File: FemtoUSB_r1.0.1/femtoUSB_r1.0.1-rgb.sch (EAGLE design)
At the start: 33 parts, among them IC1 ATSAMD21E18A-MUT

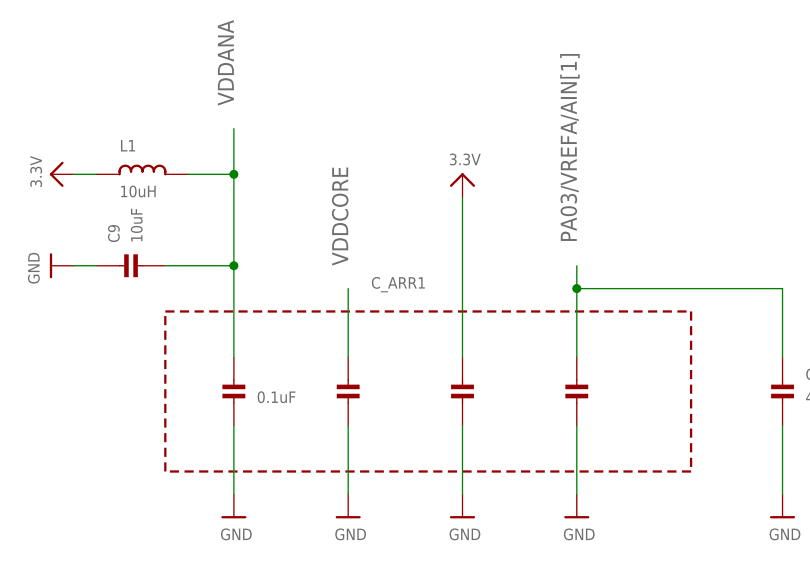
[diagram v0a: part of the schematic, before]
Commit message: Updating FemtoUSB r1.0.1 w/ RGB. Silkscreen updated to reflect Arduino pin assignments
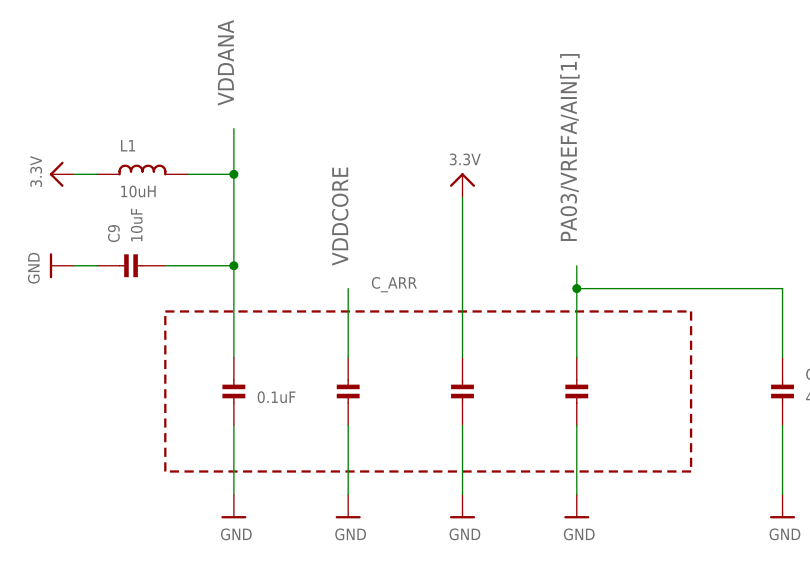
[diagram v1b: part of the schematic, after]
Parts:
- renumbered C_ARR1 to C_ARR, U$40 to OSC32K, U$43 to BTN_BOOT
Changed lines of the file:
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@@
 <part name="U$18" library="microbuilder" deviceset="GND" device=""/>
 <part name="U$19" library="microbuilder" deviceset="3.3V" device=""/>
-<part name="C_ARR1" library="array-capacitor" deviceset="KEMET_CERAMIC_CAPACITOR_ARRAY_1X4" device="" value="0.1uF"/>
+<part name="C_ARR" library="array-capacitor" deviceset="KEMET_CERAMIC_CAPACITOR_ARRAY_1X4" device="" value="0.1uF"/>
 <part name="SJ_RESET" library="femtoduino" deviceset="SPST_SMD" device="" value="OMRON B3U-300P(M)"/>
 <part name="U$17" library="microbuilder" deviceset="GND" device=""/>
@@
 <part name="C8" library="microbuilder" deviceset="CAP_CERAMIC" device="_0402MP" value="10uF"/>
 <part name="U$39" library="microbuilder" deviceset="GND" device=""/>
-<part name="U$40" library="crystals" deviceset="ABS06-107-32.768KHZ-T" device=""/>
+<part name="OSC32K" library="crystals" deviceset="ABS06-107-32.768KHZ-T" device=""/>
 <part name="C10" library="microbuilder" deviceset="CAP_CERAMIC" device="_0402MP" value="12pF"/>
 <part name="C11" library="microbuilder" deviceset="CAP_CERAMIC" device="_0402MP" value="12pF"/>
 <part name="U$41" library="microbuilder" deviceset="GND" device=""/>
 <part name="U$42" library="microbuilder" deviceset="GND" device=""/>
-<part name="U$43" library="omron_tactile_switch" deviceset="TACTILE_SWITCH_NO_GND_NO_BOSS" device=""/>
+<part name="BTN_BOOT" library="omron_tactile_switch" deviceset="TACTILE_SWITCH_NO_GND_NO_BOSS" device=""/>
 <part name="R5" library="microbuilder" deviceset="RESISTOR" device="_0402MP" value="330"/>
 <part name="R6" library="microbuilder" deviceset="RESISTOR" device="_0402MP" value="100K"/>
@@
 <instance part="U$18" gate="G$1" x="226.06" y="134.62"/>
 <instance part="U$19" gate="G$1" x="226.06" y="177.8"/>
-<instance part="C_ARR1" gate="G$1" x="180.34" y="58.42"/>
+<instance part="C_ARR" gate="G$1" x="180.34" y="58.42"/>
 <instance part="SJ_RESET" gate="G$1" x="200.66" y="147.32" rot="MR270"/>
 <instance part="U$17" gate="G$1" x="22.86" y="142.24" rot="R270"/>
@@
 <instance part="C8" gate="G$1" x="241.3" y="58.42" rot="R180"/>
 <instance part="U$39" gate="G$1" x="172.72" y="152.4" rot="R90"/>
-<instance part="U$40" gate="G$1" x="152.4" y="137.16"/>
+<instance part="OSC32K" gate="G$1" x="152.4" y="137.16"/>
 <instance part="C10" gate="G$1" x="147.32" y="132.08" rot="R180"/>
 <instance part="C11" gate="G$1" x="162.56" y="132.08" rot="R180"/>
 <instance part="U$41" gate="G$1" x="147.32" y="121.92"/>
 <instance part="U$42" gate="G$1" x="162.56" y="121.92"/>
-<instance part="U$43" gate="G$1" x="154.94" y="152.4"/>
+<instance part="BTN_BOOT" gate="G$1" x="154.94" y="152.4"/>
 <instance part="R5" gate="G$1" x="33.02" y="83.82"/>
 <instance part="R6" gate="G$1" x="43.18" y="78.74"/>
@@
 </segment>
 <segment>
-<pinref part="U$40" gate="G$1" pin="XTALIN"/>
+<pinref part="OSC32K" gate="G$1" pin="XTALIN"/>
 <wire x1="152.4" y1="137.16" x2="147.32" y2="137.16" width="0.1524" layer="91"/>
 <label x="134.62" y="139.7" size="1.778" layer="95"/>
@@
 </segment>
 <segment>
-<pinref part="U$40" gate="G$1" pin="XTALOUT"/>
+<pinref part="OSC32K" gate="G$1" pin="XTALOUT"/>
 <wire x1="157.48" y1="137.16" x2="162.56" y2="137.16" width="0.1524" layer="91"/>
 <label x="167.64" y="139.7" size="1.778" layer="95"/>
@@
 </segment>
 <segment>
-<pinref part="C_ARR1" gate="G$1" pin="P$7"/>
+<pinref part="C_ARR" gate="G$1" pin="P$7"/>
 <wire x1="198.12" y1="60.96" x2="198.12" y2="68.58" width="0.1524" layer="91"/>
 <label x="198.12" y="73.66" size="1.778" layer="95" rot="R90"/>
@@
 </segment>
 <segment>
-<pinref part="C_ARR1" gate="G$1" pin="P$1"/>
+<pinref part="C_ARR" gate="G$1" pin="P$1"/>
 <wire x1="160.02" y1="60.96" x2="160.02" y2="71.12" width="0.1524" layer="91"/>
 <label x="160.02" y="88.9" size="1.778" layer="95" rot="R90"/>
@@
 <segment>
 <label x="144.78" y="152.4" size="1.778" layer="95" rot="R180"/>
-<pinref part="U$43" gate="G$1" pin="1"/>
+<pinref part="BTN_BOOT" gate="G$1" pin="1"/>
 <wire x1="147.32" y1="152.4" x2="152.4" y2="152.4" width="0.1524" layer="91"/>
 </segment>
@@
 </segment>
 <segment>
-<pinref part="C_ARR1" gate="G$1" pin="P$3"/>
+<pinref part="C_ARR" gate="G$1" pin="P$3"/>
 <wire x1="172.72" y1="60.96" x2="172.72" y2="68.58" width="0.1524" layer="91"/>
 <label x="172.72" y="71.12" size="1.778" layer="95" rot="R90"/>
@@
 </segment>
 <segment>
-<pinref part="C_ARR1" gate="G$1" pin="P$2"/>
+<pinref part="C_ARR" gate="G$1" pin="P$2"/>
 <pinref part="U$22" gate="G$1" pin="GND"/>
 <wire x1="160.02" y1="45.72" x2="160.02" y2="53.34" width="0.1524" layer="91"/>
 </segment>
 <segment>
-<pinref part="C_ARR1" gate="G$1" pin="P$4"/>
+<pinref part="C_ARR" gate="G$1" pin="P$4"/>
 <pinref part="U$23" gate="G$1" pin="GND"/>
 <wire x1="172.72" y1="45.72" x2="172.72" y2="53.34" width="0.1524" layer="91"/>
 </segment>
 <segment>
-<pinref part="C_ARR1" gate="G$1" pin="P$6"/>
+<pinref part="C_ARR" gate="G$1" pin="P$6"/>
 <pinref part="U$24" gate="G$1" pin="GND"/>
 <wire x1="185.42" y1="45.72" x2="185.42" y2="53.34" width="0.1524" layer="91"/>
@@
 </segment>
 <segment>
-<pinref part="C_ARR1" gate="G$1" pin="P$8"/>
+<pinref part="C_ARR" gate="G$1" pin="P$8"/>
 <wire x1="198.12" y1="53.34" x2="198.12" y2="45.72" width="0.1524" layer="91"/>
 <pinref part="U$33" gate="G$1" pin="GND"/>
@@
 <pinref part="U$39" gate="G$1" pin="GND"/>
 <wire x1="162.56" y1="152.4" x2="170.18" y2="152.4" width="0.1524" layer="91"/>
-<pinref part="U$43" gate="G$1" pin="2"/>
+<pinref part="BTN_BOOT" gate="G$1" pin="2"/>
 </segment>
 <segment>
@@
 </segment>
 <segment>
-<pinref part="C_ARR1" gate="G$1" pin="P$5"/>
+<pinref part="C_ARR" gate="G$1" pin="P$5"/>
 <wire x1="185.42" y1="60.96" x2="185.42" y2="78.74" width="0.1524" layer="91"/>
 <pinref part="U$2" gate="G$1" pin="3.3V"/>

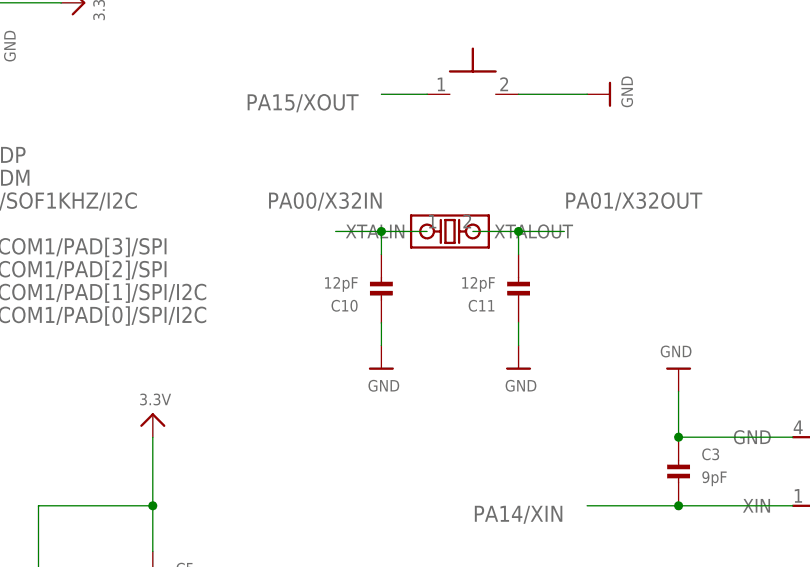
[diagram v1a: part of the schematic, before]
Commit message: Updating cap value for 32.768KHz crystal to correct value, adding in example sketches
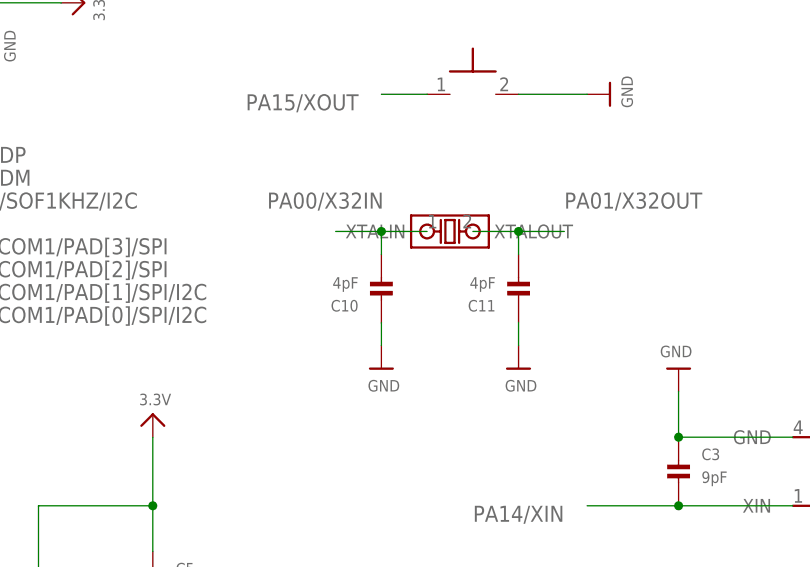
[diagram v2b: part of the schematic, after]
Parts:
- C10, C11: value 12pF -> 4pF
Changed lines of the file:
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@@
 <part name="U$39" library="microbuilder" deviceset="GND" device=""/>
 <part name="OSC32K" library="crystals" deviceset="ABS06-107-32.768KHZ-T" device=""/>
-<part name="C10" library="microbuilder" deviceset="CAP_CERAMIC" device="_0402MP" value="12pF"/>
-<part name="C11" library="microbuilder" deviceset="CAP_CERAMIC" device="_0402MP" value="12pF"/>
+<part name="C10" library="microbuilder" deviceset="CAP_CERAMIC" device="_0402MP" value="4pF"/>
+<part name="C11" library="microbuilder" deviceset="CAP_CERAMIC" device="_0402MP" value="4pF"/>
 <part name="U$41" library="microbuilder" deviceset="GND" device=""/>
 <part name="U$42" library="microbuilder" deviceset="GND" device=""/>

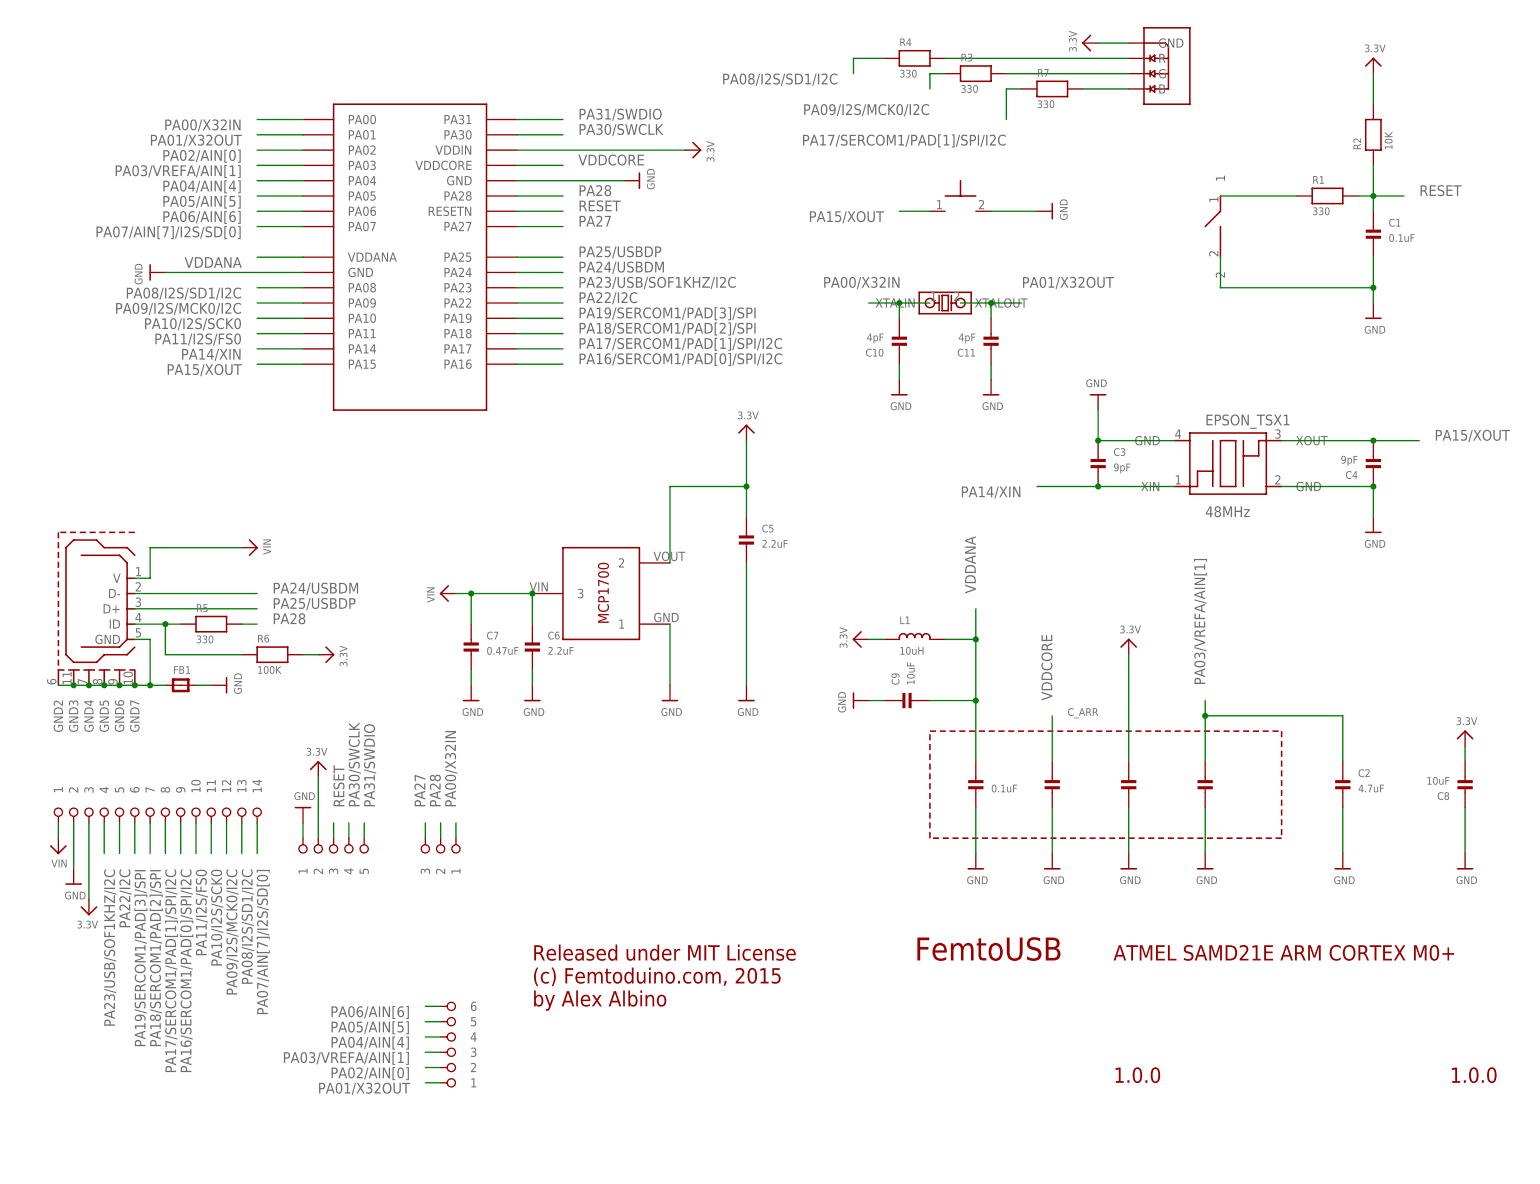
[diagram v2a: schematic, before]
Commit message: Updating Bill of Materials, and component attributes to include mfr ID. Button is now used by PA27 instead of PA15 (boot), since Arduino core doesn't need the boot pin to upload subsequent sketches
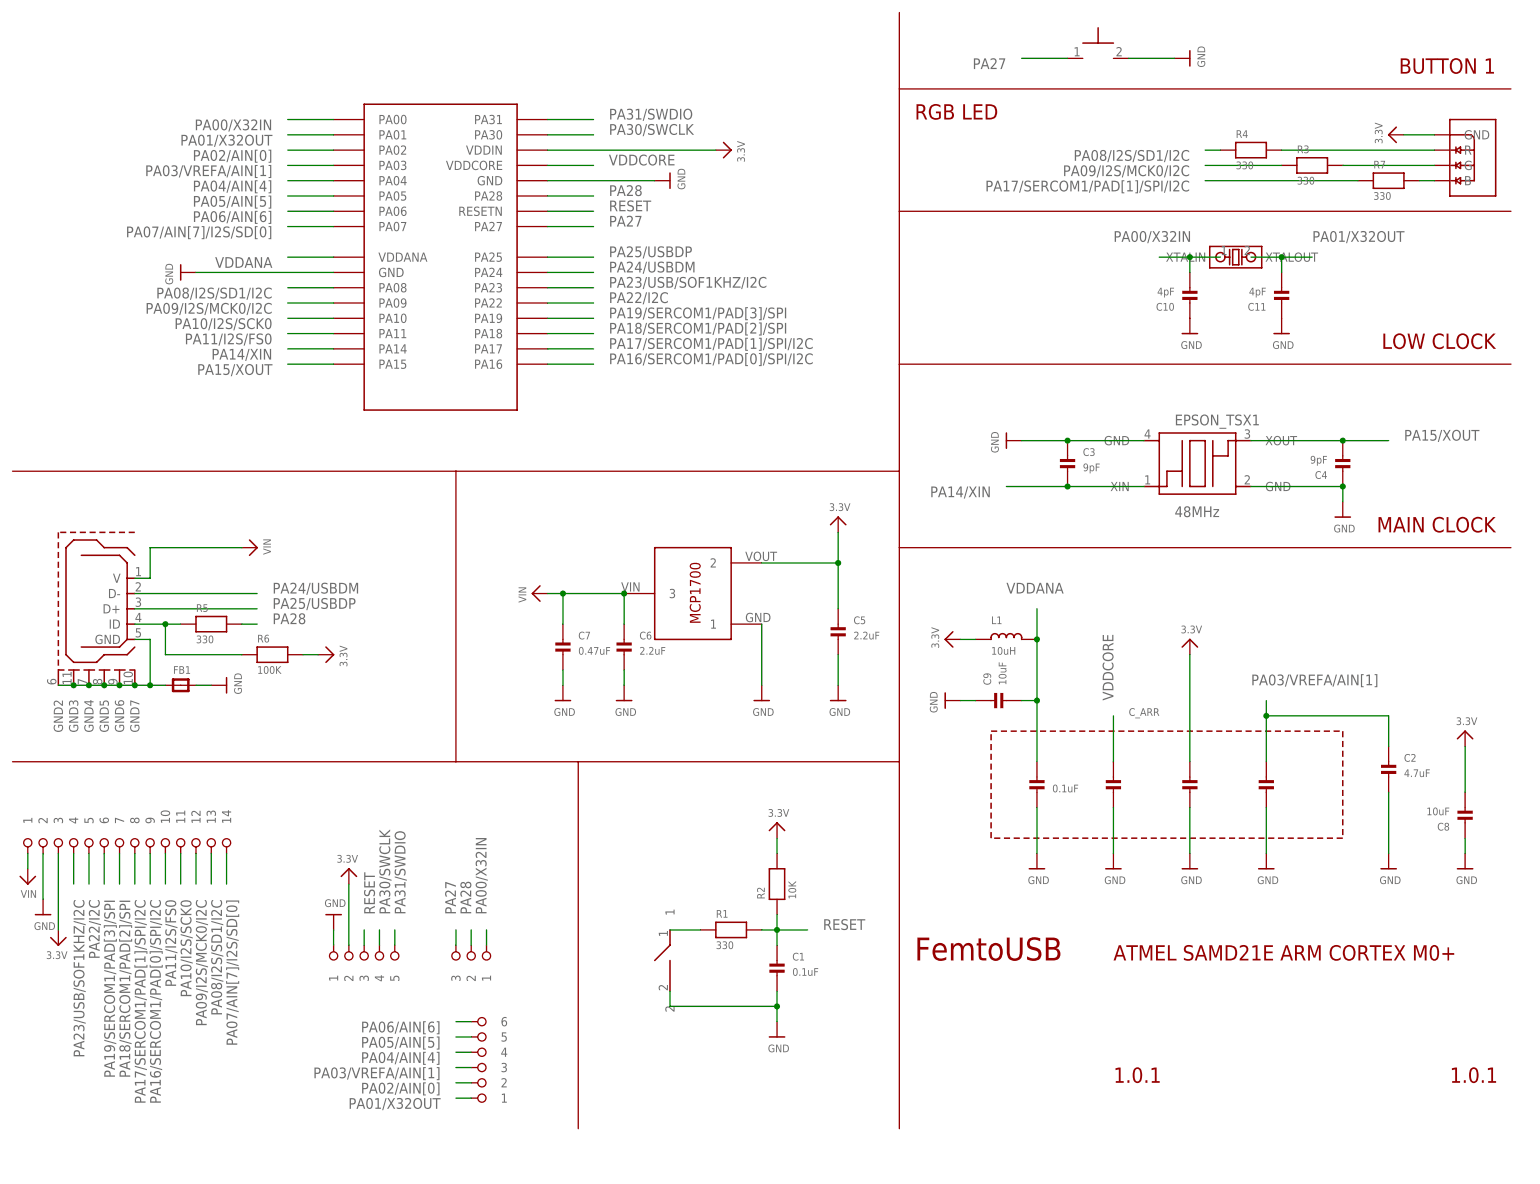
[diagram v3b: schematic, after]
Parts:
- removed U$12: 1X6_ROUND, pins_1.27mm_pitch:1X6_ROUND
- removed U$6: 1X14_ROUND, pins_1.27mm_pitch:1X14_ROUND
- removed U$7: 1X3_ROUND, pins_1.27mm_pitch:1X3_ROUND
- removed U$9: 1X5_ROUND, pins_1.27mm_pitch:1X5_ROUND
- added PIN_1X14: 1X14_ROUND, pins_1.27mm_pitch:1X14_ROUND
- added PIN_1X3: 1X3_ROUND, pins_1.27mm_pitch:1X3_ROUND
- added PIN_1X5: 1X5_ROUND, pins_1.27mm_pitch:1X5_ROUND
- added PIN_1X6: 1X6_ROUND, pins_1.27mm_pitch:1X6_ROUND
- BTN_BOOT: MFR_ID (none) -> B3U-3000PM
- C1: MFR_ID (none) -> C1005X7R1A104K050BB
- C10, C11: MFR_ID (none) -> GJM1555C1H4R0CB01D
- C2: MFR_ID (none) -> C1005X5R1A475K050BC
- C3, C4: MFR_ID (none) -> GRM0335C1E100JA01D
- C5, C6: MFR_ID (none) -> C1005X5R1C225K050BC
- C7: MFR_ID (none) -> C1005X5R1C474K050BC
- C8, C9: MFR_ID (none) -> CL05A106MP5NUNC
- C_ARR: MFR_ID (none) -> CA064C104K4RACTU
- EPSON_TSX1: DIGIKEY_PART TSX-3225 32.0000MF15X-B-ND -> (none); MFR_ID (none) -> FA-238 48.0000MB-K3
- FB1: MFR_ID (none) -> BLM18RK102SN1D
- IC1: MFR_ID (none) -> ATSAMD21E18A-MUT
- L1: MFR_ID (none) -> LQM18FN100M00D
- LDO_VREG: MFR_ID (none) -> MCP1700T-3302E/TT
- MICRO_B_USB: MFR_ID (none) -> ZX62-B-5PA(11)
- OSC32K: MFR_ID (none) -> ABS06-107-32.768kHz-T
- R1, R3, R4, R5, R7: MFR_ID (none) -> CRCW0402330RJNED
- R2: MFR_ID (none) -> CRCW040210K0JNEDHP
- R6: MFR_ID (none) -> ERJ-2RKF1003X
- RGBLED: MFR_ID (none) -> LRTB R48G
- SJ_RESET: value OMRON B3U-300P(M) -> SPST_SMD
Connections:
- net 3.3V: now also PIN_1X14.3, PIN_1X5.2; no longer U$6.3, U$9.2
- net GND: now also PIN_1X14.2, PIN_1X5.1; no longer U$6.2, U$9.1
- net PA00/X32IN: now also PIN_1X3.1; no longer U$7.1
- net PA01/X32OUT: now also PIN_1X6.1; no longer U$12.1
- net PA02/AIN[0]: now also PIN_1X6.2; no longer U$12.2
- net PA03/VREFA/AIN[1]: now also PIN_1X6.3; no longer U$12.3
- net PA04/AIN[4]: now also PIN_1X6.4; no longer U$12.4
- net PA05/AIN[5]: now also PIN_1X6.5; no longer U$12.5
- net PA06/AIN[6]: now also PIN_1X6.6; no longer U$12.6
- net PA07/AIN[7]/I2S/SD[0]: now also PIN_1X14.14; no longer U$6.14
- net PA08/I2S/SD1/I2C: now also PIN_1X14.13; no longer U$6.13
- net PA09/I2S/MCK0/I2C: now also PIN_1X14.12; no longer U$6.12
- net PA10/I2S/SCK0: now also PIN_1X14.11; no longer U$6.11
- net PA11/I2S/FS0: now also PIN_1X14.10; no longer U$6.10
- net PA15/XOUT: no longer BTN_BOOT.1
- net PA16/SERCOM1/PAD[0]/SPI/I2C: now also PIN_1X14.9; no longer U$6.9
- net PA17/SERCOM1/PAD[1]/SPI/I2C: now also PIN_1X14.8; no longer U$6.8
- net PA18/SERCOM1/PAD[2]/SPI: now also PIN_1X14.7; no longer U$6.7
- net PA19/SERCOM1/PAD[3]/SPI: now also PIN_1X14.6; no longer U$6.6
- net PA22/I2C: now also PIN_1X14.5; no longer U$6.5
- net PA23/USB/SOF1KHZ/I2C: now also PIN_1X14.4; no longer U$6.4
- net PA27: now also BTN_BOOT.1, PIN_1X3.3; no longer U$7.3
- net PA28: now also PIN_1X3.2; no longer U$7.2
- net PA30/SWCLK: now also PIN_1X5.4; no longer U$9.4
- net PA31/SWDIO: now also PIN_1X5.5; no longer U$9.5
- net RESET: now also PIN_1X5.3; no longer U$9.3
- net VIN: now also PIN_1X14.1; no longer U$6.1
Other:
- note added: "1.0.1"
- note added: "BUTTON 1"
- note added: "LOW CLOCK"
- note added: "MAIN CLOCK"
- note added: "RGB LED"
- note removed: "1.0.0"
- note removed: "Released under MIT License (c) Femtoduino.com, 2015 by Alex Albino"
- moved on the sheet: C1, C10, C11, C2, C3, C4, C5, C6, C7, C8, C9, C_ARR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
